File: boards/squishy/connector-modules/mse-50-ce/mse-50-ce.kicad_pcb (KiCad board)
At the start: 6 copper layers, 75 x 55 mm, 18 parts, among them J1 SCSI PHY Mezz, J2 Conn_02x25_Odd_Even, J3 Conn_01x04, U1 M24C02-RMC

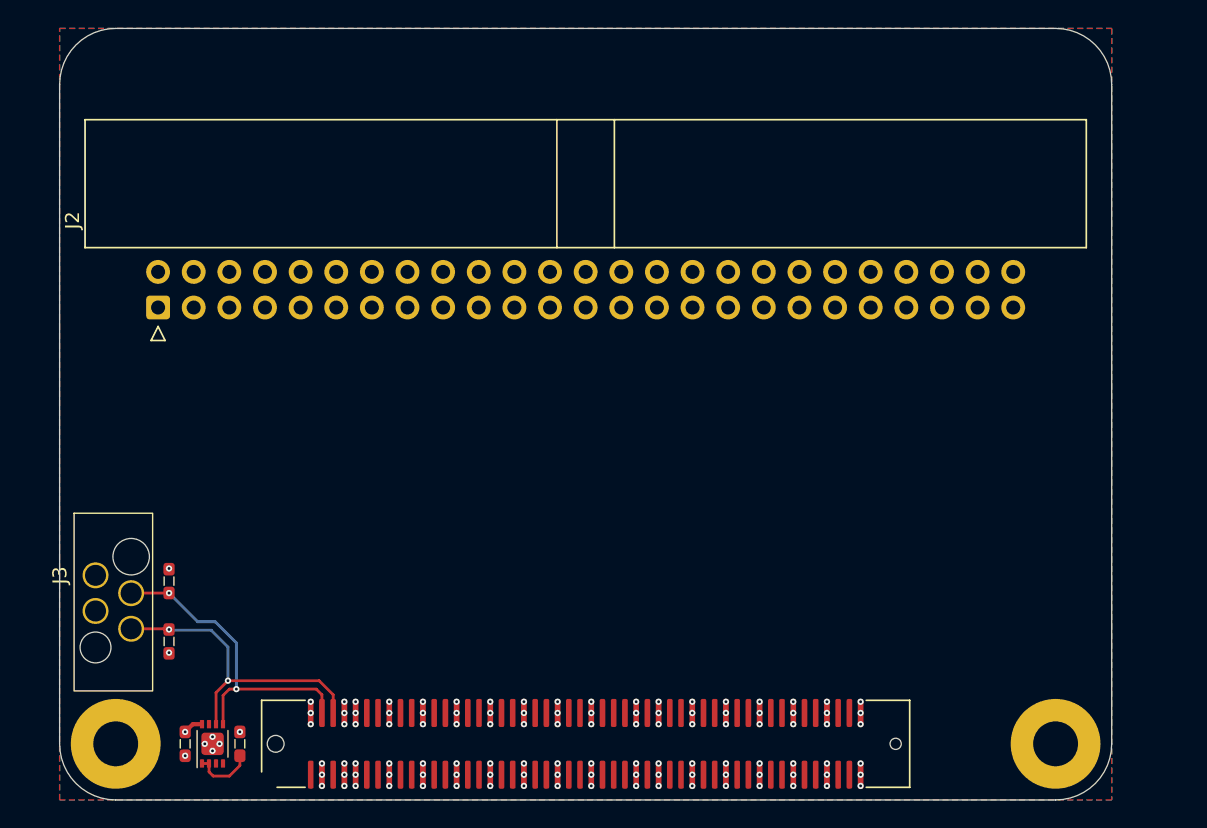
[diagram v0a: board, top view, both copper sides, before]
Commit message: squishy: connectors: Propagated changes from mse-68-hd PCB and DRC rules to mse-50-ce
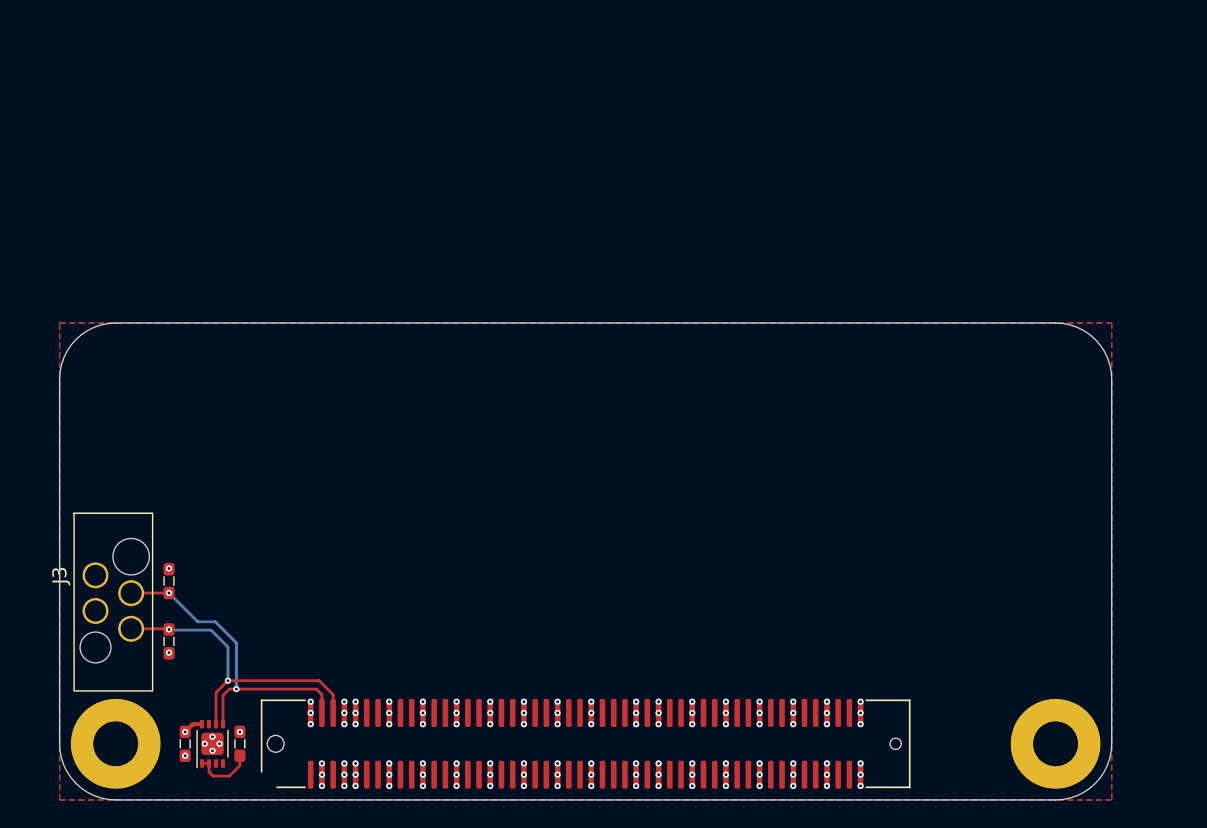
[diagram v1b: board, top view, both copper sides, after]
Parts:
- removed J2: Conn_02x25_Odd_Even, Connector_IDC:IDC-Header_2x25_P2.54mm_Horizontal
- moved REF** 21.0 mm to (121.0, 105.8)
- moved REF** 21.0 mm to (174.0, 105.8)
- moved REF** 16.2 mm to (109.7, 115.0)
- moved REF** 16.2 mm to (185.2, 115.0)
- moved REF** 4.75 mm to (185.2, 131.0)
- moved REF** 4.75 mm to (109.7, 131.0)
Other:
- board size 75 x 55 mm -> 75 x 34 mm
- board text added: "0.2028mm"
- board text added: "0.2104mm"
- board text added: "0.4000mm"
- board text added: "IFF JLCPCB: JLC06161H-7628"
- board text added: "Impedance Table: 50Ω Coplanar Single Ended (inner): width: TODO 72Ω Coplanar Single Ended (outter): width: 0.1115mm 72Ω Non-Coplanar Single Ended (outter): width: 0.1514mm 50Ω Non-Coplanar Single Ended (inner): width: TODO 120Ω Coplanar Differential (outter): width: 0.1148, space: 0.2mm 120Ω Non-Coplanar Differential (outter): width: 0.1275, space: 0.2mm"
- board text added: "Outter Copper: 1oz Inner Copper: 0.5oz"
- board text added: "Prepreg (7628*1)"
- board text removed: "0.0994mm"
- board text removed: "0.1088mm"
- board text removed: "0.5500mm"
- board text removed: "IFF JLCPCB: JLC06161H-3313"
- board text removed: "Impedance Table: 50Ω Coplanar Signle Ended (inner): width: TODO 50Ω Coplanar Signle Ended (outter): width: TODO 50Ω Non-Coplanar Signle Ended (inner): width: TODO 50Ω Non-Coplanar Signle Ended (outter): width: TODO"
- board text removed: "Outter Copper: 1Oz Inner Copper: 0.5Oz"
- board text removed: "Prepreg (2116*1)"
- board text removed: "Prepreg (3313*1)"

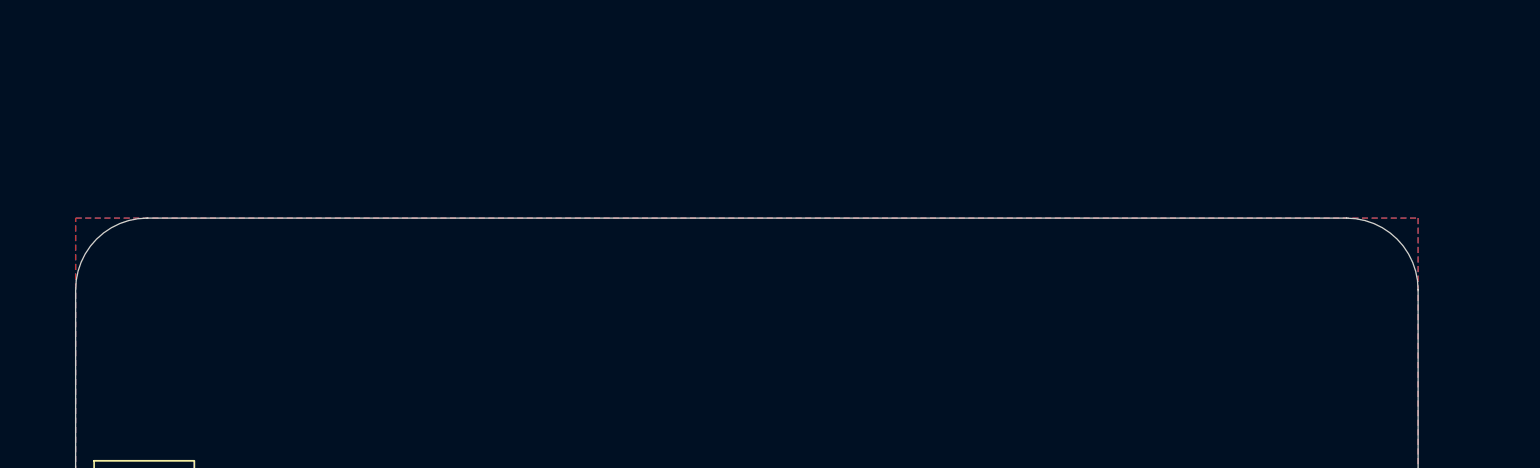
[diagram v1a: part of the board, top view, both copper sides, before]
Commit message: squishy: connectors: hooked up mse-50-ce connector
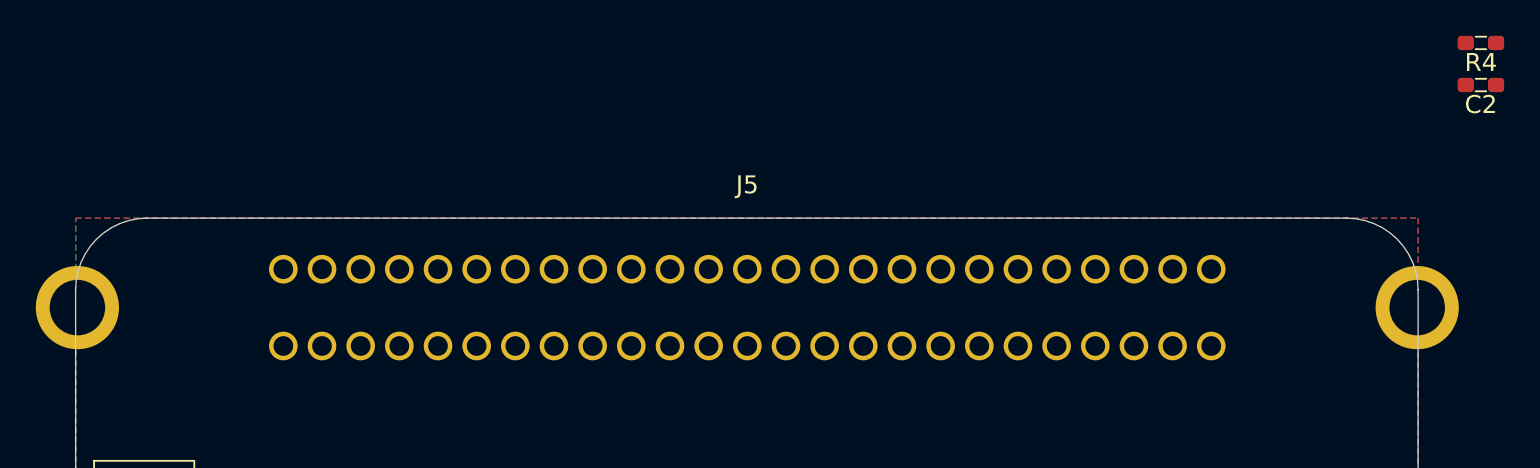
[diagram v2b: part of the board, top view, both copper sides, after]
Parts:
- added C2: 100n, rhais_rcl:C0603, F.Cu at (188.5, 98.6)
- added J5: Centronics 50, lethalbit-connectors:112-050-213R001, F.Cu at (147.5, 111.0)
- added R4: 1M, rhais_rcl:R0603, F.Cu at (188.5, 96.2)

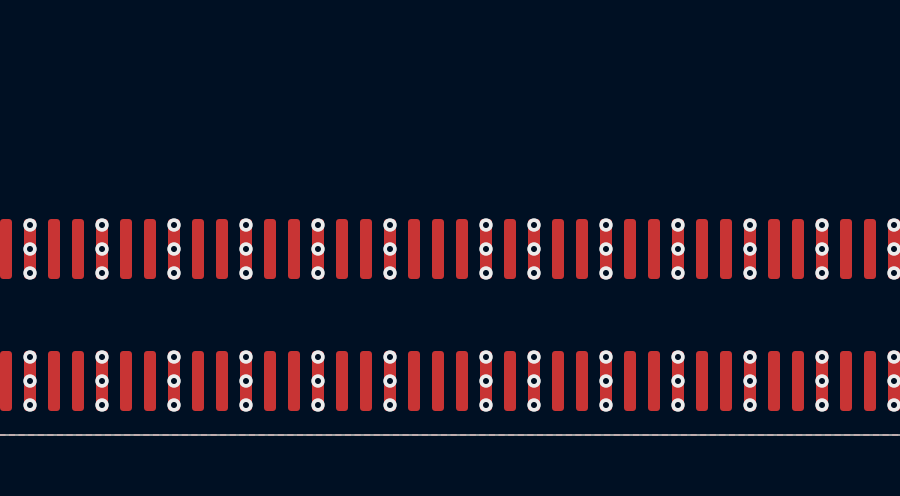
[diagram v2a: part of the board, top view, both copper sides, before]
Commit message: squishy: connectors: Fixed the pour layers and added TERMPWR stitching for mse-50-ce
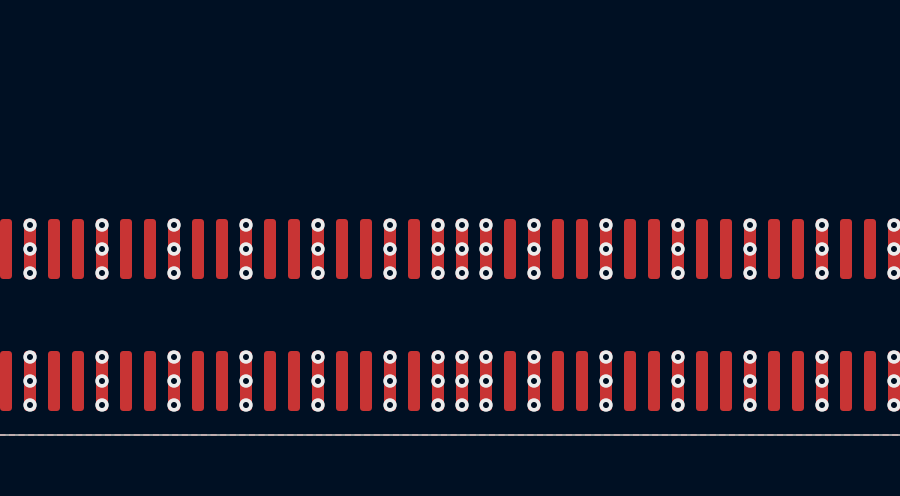
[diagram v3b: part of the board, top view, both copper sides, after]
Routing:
- net /CON.TERMPWR: vias 0 -> 12
- added copper zone on In2.Cu, net +3V3
- added copper zone on In2.Cu, net /CON.TERMPWR
- removed copper zone on In1.Cu, net +3V3
- removed copper zone on In2.Cu, net GND

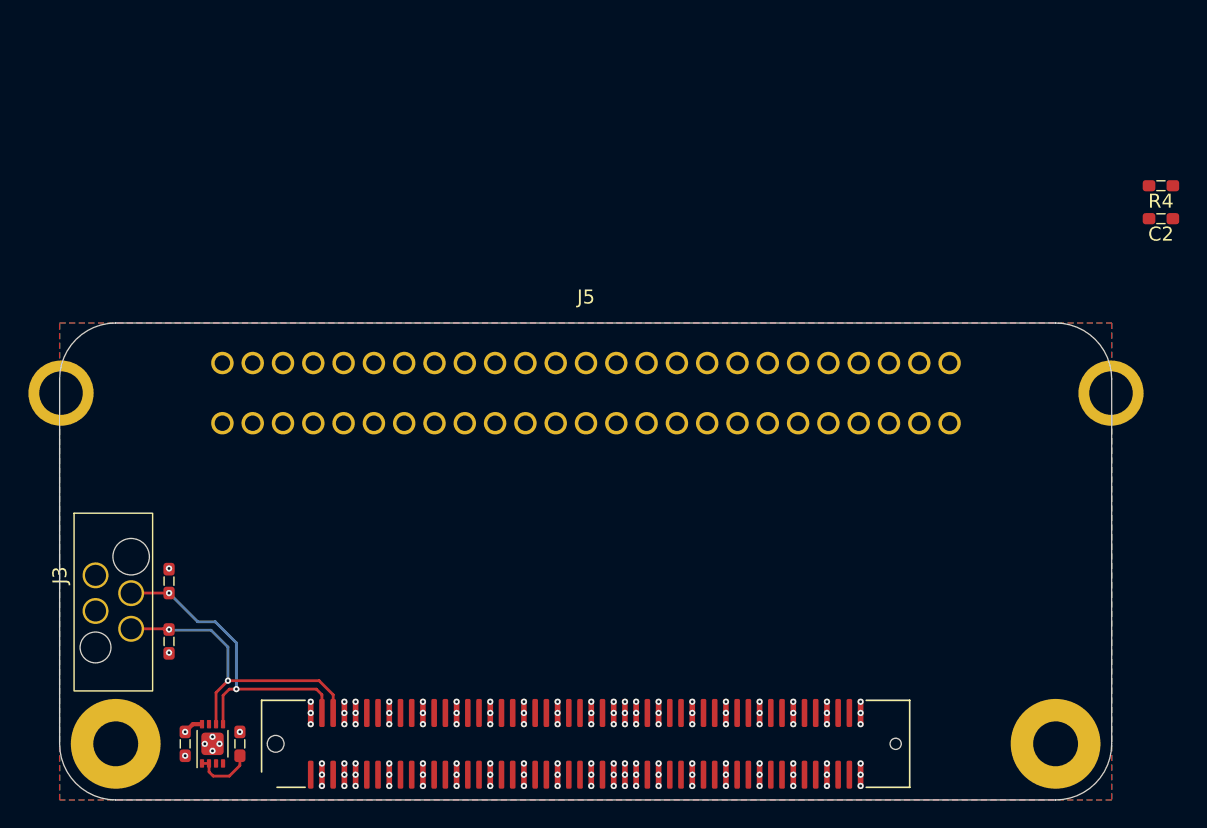
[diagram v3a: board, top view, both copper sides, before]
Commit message: squishy: connectors: Adjusted the CE-50 connector to have a less conservative courtyard to allow us scoot the connector back for more board support.
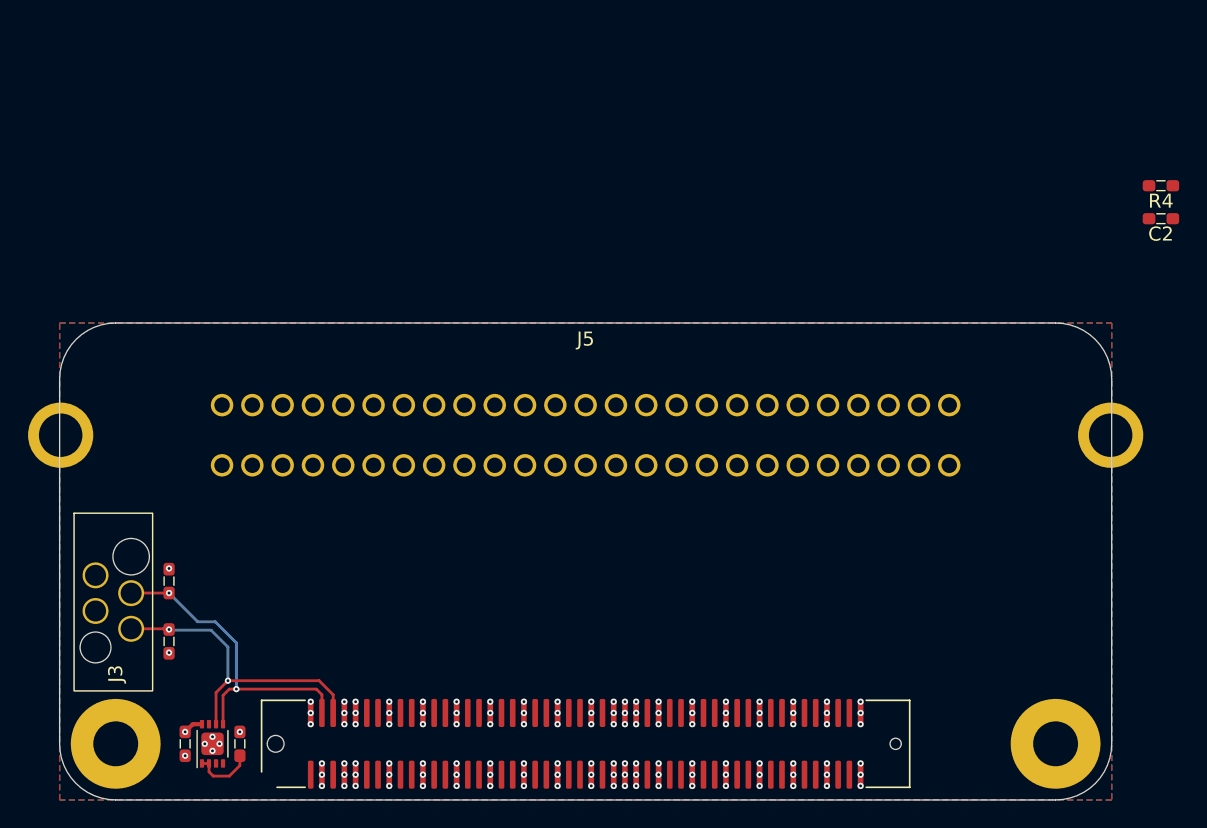
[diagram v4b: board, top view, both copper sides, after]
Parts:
- moved J5 3.00 mm to (147.5, 114.0)
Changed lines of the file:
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@@
 	(footprint "lethalbit-connectors:112-050-213R001"
 		(layer "F.Cu")
-		(at 147.525 111 180)
+		(at 147.5 114 180)
 		(descr "Norcomp 50-pin Centronics Connector")
 		(property "Reference" "J5"
@@
 		)
 		(fp_line
-			(start 42.5 -8.2)
+			(start 42.5 -5.3)
 			(end 42.5 10.7)
 			(stroke
@@
 		(fp_line
 			(start -42.5 10.7)
-			(end -42.5 -8.2)
+			(end -42.5 -5.3)
 			(stroke
 				(width 0.12)
@@
 		)
 		(fp_line
-			(start -42.5 -8.2)
-			(end 42.5 -8.2)
+			(start -42.5 -5.3)
+			(end 42.5 -5.3)
 			(stroke
 				(width 0.12)
@@
 		)
 		(fp_line
-			(start -39.45 10.7)
-			(end 39.45 10.7)
+			(start 32.1 19.2)
+			(end 32.1 10.7)
+			(stroke
+				(width 0.1)
+				(type default)
+			)
+			(layer "F.Fab")
+		)
+		(fp_line
+			(start 32.1 19.2)
+			(end -32 19.2)
+			(stroke
+				(width 0.1)
+				(type default)
+			)
+			(layer "F.Fab")
+		)
+		(fp_line
+			(start -32 19.2)
+			(end -32 10.7)
+			(stroke
+				(width 0.1)
+				(type default)
+			)
+			(layer "F.Fab")
+		)
+		(fp_line
+			(start -44 10.6)
+			(end 44 10.6)
 			(stroke
 				(width 0.12)
@@
 		)
 		(pad "3" thru_hole circle
-			(at 21.6 -2.145001 180)
+			(at 21.6 -2.145 180)
 			(size 1.6 1.6)
 			(drill 1.1)
@@
 		)
 		(pad "6" thru_hole circle
-			(at 15.12 -2.145001 180)
+			(at 15.12 -2.145 180)
 			(size 1.6 1.6)
 			(drill 1.1)
@@
 		)
 		(pad "9" thru_hole circle
-			(at 8.640001 -2.145 180)
+			(at 8.64 -2.145 180)
 			(size 1.6 1.6)
 			(drill 1.1)
@@
 		)
 		(pad "17" thru_hole circle
-			(at -8.640001 -2.145 180)
+			(at -8.64 -2.145 180)
 			(size 1.6 1.6)
 			(drill 1.1)
@@
 		)
 		(pad "20" thru_hole circle
-			(at -15.12 -2.145001 180)
+			(at -15.12 -2.145 180)
 			(size 1.6 1.6)
 			(drill 1.1)
@@
 		)
 		(pad "23" thru_hole circle
-			(at -21.6 -2.145001 180)
+			(at -21.6 -2.145 180)
 			(size 1.6 1.6)
 			(drill 1.1)
@@
 		)
 		(pad "28" thru_hole circle
-			(at 21.6 2.145001 180)
+			(at 21.6 2.145 180)
 			(size 1.6 1.6)
 			(drill 1.1)
@@
 		)
 		(pad "31" thru_hole circle
-			(at 15.12 2.145001 180)
+			(at 15.12 2.145 180)
 			(size 1.6 1.6)
 			(drill 1.1)
@@
 		)
 		(pad "34" thru_hole circle
-			(at 8.640001 2.145 180)
+			(at 8.64 2.145 180)
 			(size 1.6 1.6)
 			(drill 1.1)
@@
 		)
 		(pad "42" thru_hole circle
-			(at -8.640001 2.145 180)
+			(at -8.64 2.145 180)
 			(size 1.6 1.6)
 			(drill 1.1)
@@
 		)
 		(pad "45" thru_hole circle
-			(at -15.12 2.145001 180)
+			(at -15.12 2.145 180)
 			(size 1.6 1.6)
 			(drill 1.1)
@@
 		)
 		(pad "48" thru_hole circle
-			(at -21.6 2.145001 180)
+			(at -21.6 2.145 180)
 			(size 1.6 1.6)
 			(drill 1.1)
@@
 			(pintype "power_in")
 		)
-		(model "${EDALIBS}/lethalbit-connectors.3dshapes/112-050-113R001.wrz"
+		(model "${EDALIBS}/lethalbit-connectors.3dshapes/112-050-213R001.STEP"
 			(offset
 				(xyz 0 -11 8)
@@
 		(descr "WR-WST REDFIT IDC - SKEDD - Spring Connector - debug")
 		(property "Reference" "J3"
-			(at 0 -2.54 90)
+			(at -7.01 1.44 90)
 			(unlocked yes)
 			(layer "F.SilkS")
